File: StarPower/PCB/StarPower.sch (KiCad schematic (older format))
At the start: 16 parts, among them SW1 TL3301, U1 ATtiny25-20SSU, U2 SGM809B-SXN3LG, U3 PAM2804AAB010, Y1 32.768 kHz

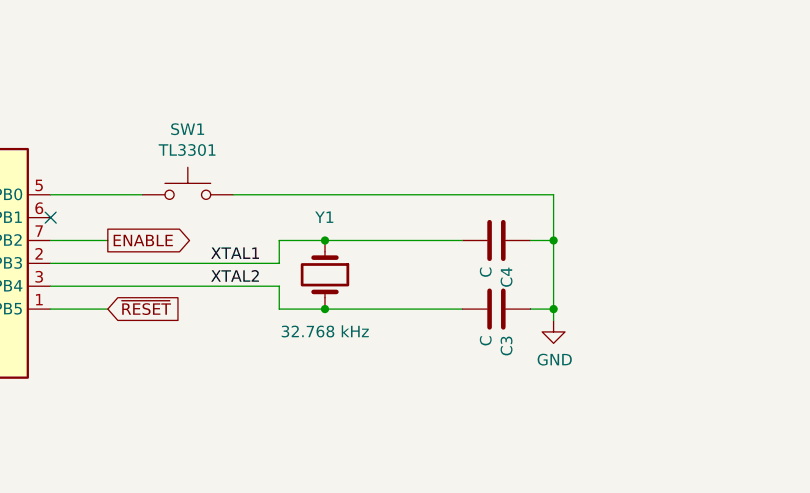
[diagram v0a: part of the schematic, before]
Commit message: Remove C4 & C5, the load capacitors at the crystal.
The internal capacitance of the ATtinyx5 is enough.
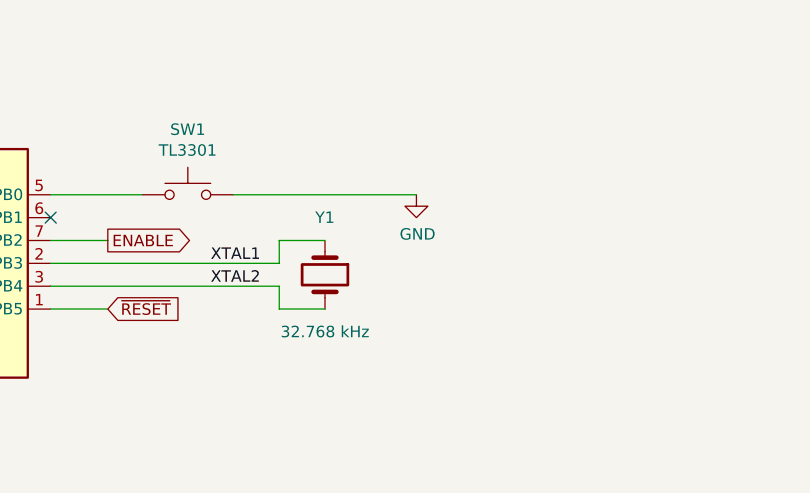
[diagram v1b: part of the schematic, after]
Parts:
- removed C3, C4: C, Capacitor_SMD:C_0805_2012Metric_Pad1.18x1.45mm_HandSolder, symbol Device:C
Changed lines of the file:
@@
-$EndComp
-$Comp
-L Device:C C3
-U 1 1 6369D795
-P 5350 5500
-F 0 "C3" H 5465 5546 50  0000 L CNN
-F 1 "C" H 5465 5455 50  0000 L CNN
-F 2 "Capacitor_SMD:C_0805_2012Metric_Pad1.18x1.45mm_HandSolder" H 5388 5350 50  0001 C CNN
-F 3 "~" H 5350 5500 50  0001 C CNN
-	1    5350 5500
-	0    1    1    0
-$EndComp
-$Comp
-L Device:C C4
-U 1 1 6369DFE7
-P 5350 5200
-F 0 "C4" H 5465 5246 50  0000 L CNN
-F 1 "C" H 5465 5155 50  0000 L CNN
-F 2 "Capacitor_SMD:C_0805_2012Metric_Pad1.18x1.45mm_HandSolder" H 5388 5050 50  0001 C CNN
-F 3 "~" H 5350 5200 50  0001 C CNN
-	1    5350 5200
-	0    1    1    0
 $EndComp
 $Comp
@@
 L power:GND #PWR0104
 U 1 1 636C6851
-P 5600 5550
-F 0 "#PWR0104" H 5600 5300 50  0001 C CNN
-F 1 "GND" H 5605 5377 50  0000 C CNN
-F 2 "" H 5600 5550 50  0001 C CNN
-F 3 "" H 5600 5550 50  0001 C CNN
-	1    5600 5550
-	1    0    0    -1
-$EndComp
-Wire Wire Line
-	5600 5550 5600 5500
-Wire Wire Line
-	5600 5500 5600 5200
-Wire Wire Line
-	5600 5200 5500 5200
-Wire Wire Line
-	5500 5500 5600 5500
+P 5000 5000
+F 0 "#PWR0104" H 5000 4750 50  0001 C CNN
+F 1 "GND" H 5005 4827 50  0000 C CNN
+F 2 "" H 5000 5000 50  0001 C CNN
+F 3 "" H 5000 5000 50  0001 C CNN
+	1    5000 5000
+	1    0    0    -1
+$EndComp
 Wire Wire Line
 	6850 3200 6850 3100
@@
 Wire Wire Line
 	2800 4650 2800 4700
-Connection ~ 5600 5500
-Wire Wire Line
-	5600 5200 5600 5000
-Wire Wire Line
-	5600 5000 4200 5000
-Connection ~ 5600 5200
+Wire Wire Line
+	5000 5000 4200 5000
 Wire Wire Line
 	3800 5000 3400 5000
@@
 Wire Wire Line
 	4400 5200 4600 5200
-Connection ~ 4600 5200
-Wire Wire Line
-	4600 5200 5200 5200
-Connection ~ 4600 5500
-Wire Wire Line
-	4600 5500 5200 5500
 Wire Wire Line
 	4550 3600 5600 3600

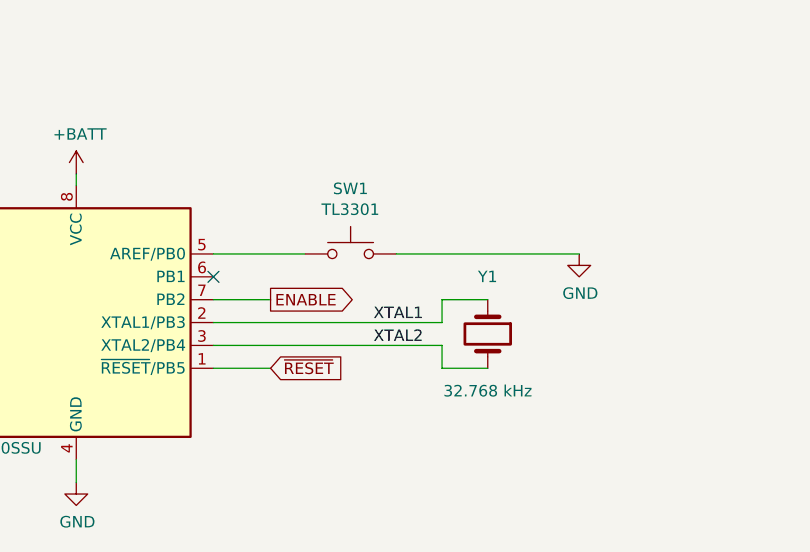
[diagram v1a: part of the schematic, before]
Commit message: Connect PB1 of U1 to Ground (see ebe2459f).
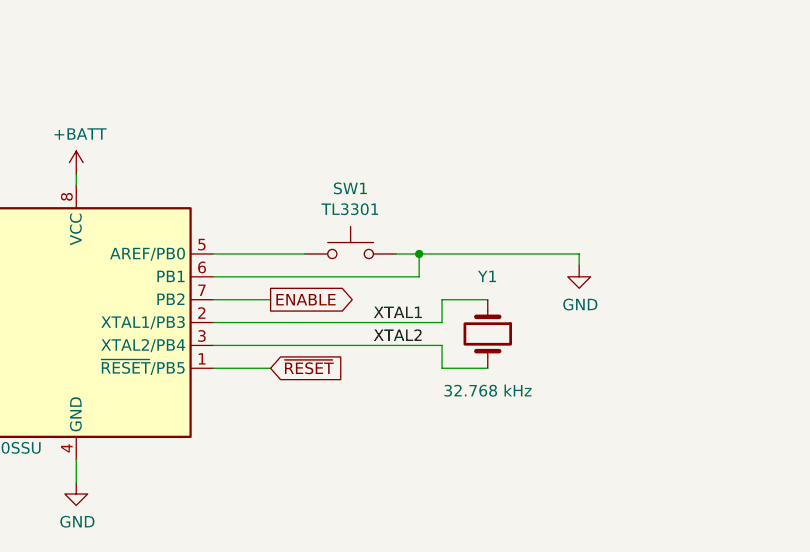
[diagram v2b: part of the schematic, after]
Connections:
- net GND: now also U1.6 (PB1)
- no-connect marks 1 -> 0
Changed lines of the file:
@@
 Wire Wire Line
 	4400 5300 3400 5300
-$Comp
-L power:GND #PWR0104
-U 1 1 636C6851
-P 5000 5000
-F 0 "#PWR0104" H 5000 4750 50  0001 C CNN
-F 1 "GND" H 5005 4827 50  0000 C CNN
-F 2 "" H 5000 5000 50  0001 C CNN
-F 3 "" H 5000 5000 50  0001 C CNN
-	1    5000 5000
-	1    0    0    -1
-$EndComp
 Wire Wire Line
 	6850 3200 6850 3100
@@
 	2800 4650 2800 4700
 Wire Wire Line
-	5000 5000 4200 5000
-Wire Wire Line
 	3800 5000 3400 5000
-NoConn ~ 3400 5100
 Connection ~ 6850 3600
 Connection ~ 6850 2700
@@
 	1    0    0    -1
 $EndComp
+Wire Wire Line
+	3400 5100 4300 5100
+Wire Wire Line
+	4300 5100 4300 5000
+Connection ~ 4300 5000
+Wire Wire Line
+	4300 5000 4200 5000
+Wire Wire Line
+	5000 5050 5000 5000
+Wire Wire Line
+	5000 5000 4300 5000
+$Comp
+L power:GND #PWR0104
+U 1 1 636C6851
+P 5000 5050
+F 0 "#PWR0104" H 5000 4800 50  0001 C CNN
+F 1 "GND" H 5005 4877 50  0000 C CNN
+F 2 "" H 5000 5050 50  0001 C CNN
+F 3 "" H 5000 5050 50  0001 C CNN
+	1    5000 5050
+	1    0    0    -1
+$EndComp

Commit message: Changed microcontroller footprint of U1, and using the low voltage type now.
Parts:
- U1: value ATtiny25-20SSU -> ATtiny25V-10SU; footprint Package_SO:SOIC-8_3.9x4.9mm_P1.27mm -> Package_SO:SOIJ-8_5.3x5.3mm_P1.27mm; symbol MCU_Microchip_ATtiny:ATtiny25-20SSU -> MCU_Microchip_ATtiny:ATtiny25V-10SU
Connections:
- net BUTTON: now reaches SW1.1, U1.5 (AREF/PB0)
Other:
- moved on the sheet: SW1
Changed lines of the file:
@@
 $EndComp
 $Comp
-L MCU_Microchip_ATtiny:ATtiny25-20SSU U1
+L MCU_Microchip_ATtiny:ATtiny25V-10SU U1
 U 1 1 6369BBC6
 P 2800 5300
-F 0 "U1" H 2400 5850 50  0000 R CNN
-F 1 "ATtiny25-20SSU" H 2650 4750 50  0000 R CNN
-F 2 "Package_SO:SOIC-8_3.9x4.9mm_P1.27mm" H 2800 5300 50  0001 C CIN
+F 0 "U1" H 2300 5850 50  0000 L CNN
+F 1 "ATtiny25V-10SU" H 2650 4750 50  0000 R CNN
+F 2 "Package_SO:SOIJ-8_5.3x5.3mm_P1.27mm" H 2800 5300 50  0001 C CIN
 F 3 "http://ww1.microchip.com/downloads/en/DeviceDoc/atmel-2586-avr-8-bit-microcontroller-attiny25-attiny45-attiny85_datasheet.pdf" H 2800 5300 50  0001 C CNN
 	1    2800 5300
@@
 L Switch:SW_Push SW1
 U 1 1 636A2B0E
-P 4000 5000
-F 0 "SW1" H 4000 5285 50  0000 C CNN
-F 1 "TL3301" H 4000 5194 50  0000 C CNN
-F 2 "mibe:SW_SPST_TL3301" H 4000 5200 50  0001 C CNN
-F 3 "~" H 4000 5200 50  0001 C CNN
-	1    4000 5000
+P 4150 5000
+F 0 "SW1" H 4150 5285 50  0000 C CNN
+F 1 "TL3301" H 4150 5194 50  0000 C CNN
+F 2 "mibe:SW_SPST_TL3301" H 4150 5200 50  0001 C CNN
+F 3 "~" H 4150 5200 50  0001 C CNN
+	1    4150 5000
 	1    0    0    -1
 $EndComp
@@
 	2800 4650 2800 4700
 Wire Wire Line
-	3800 5000 3400 5000
+	3950 5000 3400 5000
 Connection ~ 6850 3600
 Connection ~ 6850 2700
@@
 $EndComp
 Wire Wire Line
-	3400 5100 4300 5100
-Wire Wire Line
-	4300 5100 4300 5000
-Connection ~ 4300 5000
-Wire Wire Line
-	4300 5000 4200 5000
+	3400 5100 4400 5100
+Wire Wire Line
+	4400 5100 4400 5000
+Connection ~ 4400 5000
+Wire Wire Line
+	4400 5000 4350 5000
 Wire Wire Line
 	5000 5050 5000 5000
 Wire Wire Line
-	5000 5000 4300 5000
+	5000 5000 4400 5000
 $Comp
 L power:GND #PWR0104
@@
 	1    0    0    -1
 $EndComp
+Text Label 3650 5000 0    50   ~ 0
+BUTTON
 $EndSCHEMATC
